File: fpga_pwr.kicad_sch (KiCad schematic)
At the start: 29 parts, among them Q1 BC817, U8 LFE5U-25F-8MG285C

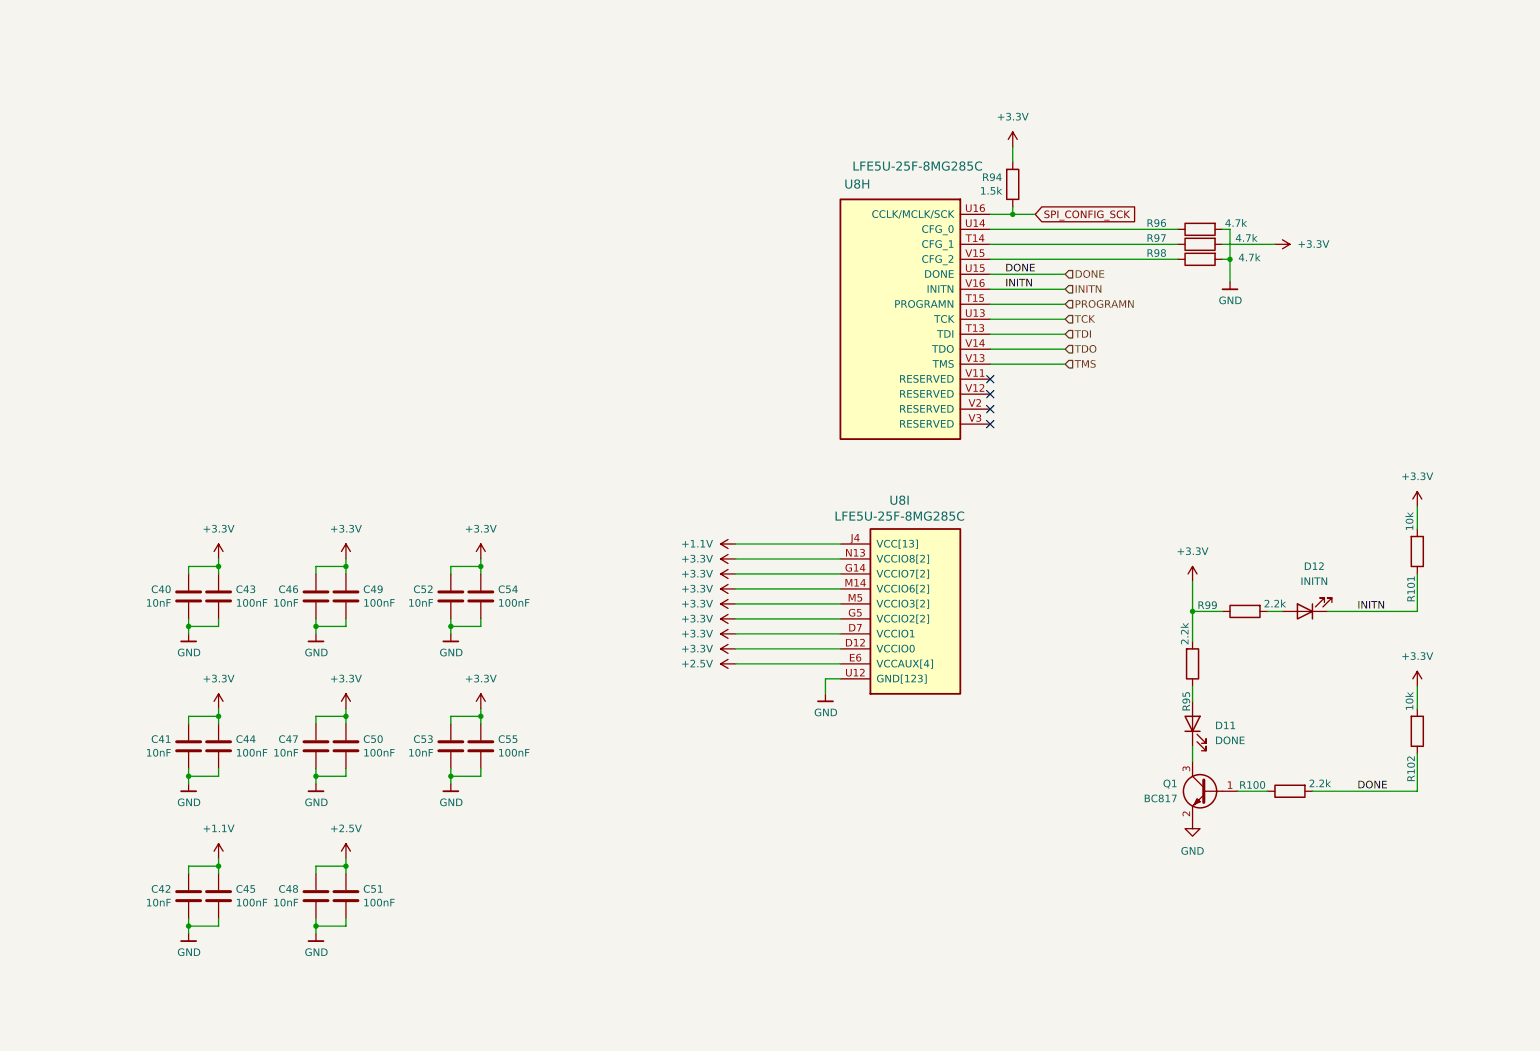
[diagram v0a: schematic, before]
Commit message: Changa fpga footprint to bg256. Update project
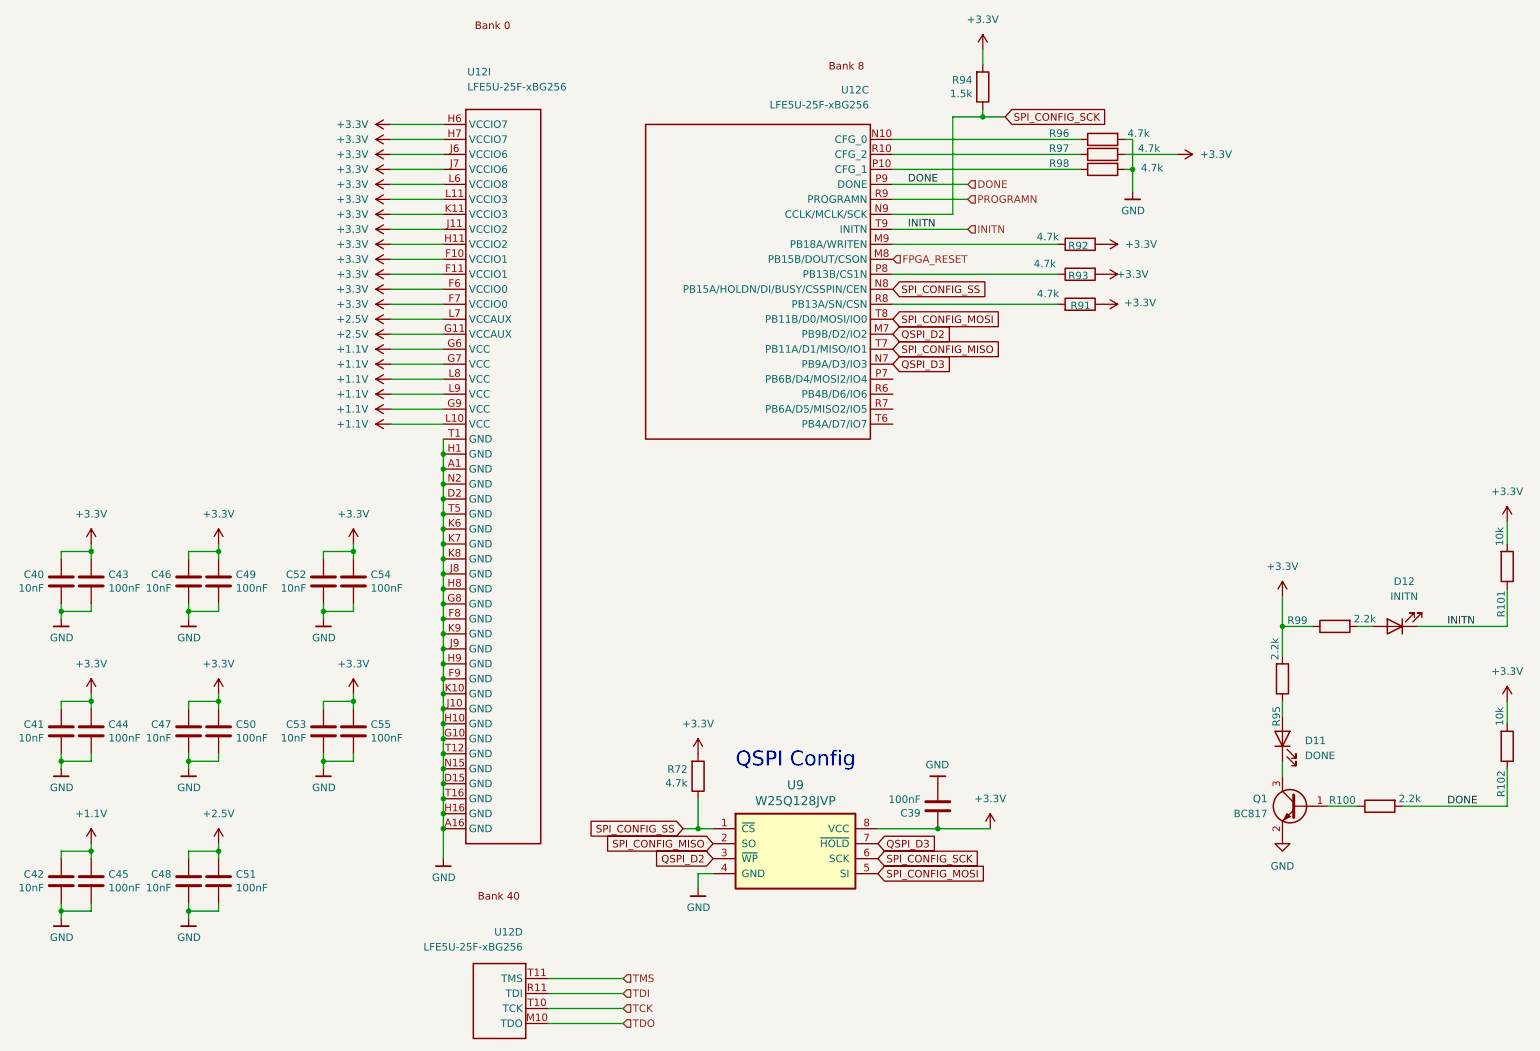
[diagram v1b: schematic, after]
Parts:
- removed U8: LFE5U-25F-8MG285C, kicad:BGA-285, symbol gkl_lattice:ECP5U25-MG285
- added C39: 100nF, Capacitor_SMD:C_0603_1608Metric, symbol Device:C
- added R72, R91, R92, R93: 4.7k, Resistor_SMD:R_0603_1608Metric, symbol Device:R
- added U12: LFE5U-25F-xBG256, EasyEDA_Lib:CABGA-256_L14.0-W14.0-R16-C16-P0.80-TL, symbol asterix:LFE5U-25F-BG256
- added U9: W25Q128JVP, Package_SON:WSON-8-1EP_6x5mm_P1.27mm_EP3.4x4mm, symbol gkl_mem:AT25SF081
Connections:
- net +1.1V: now also U12.G6 (VCC), U12.G7 (VCC), U12.G9 (VCC), U12.L10 (VCC), U12.L8 (VCC), U12.L9 (VCC)
- net +2.5V: now also U12.G11 (VCCAUX), U12.L7 (VCCAUX)
- net +3.3V: now also C39.1, R72.2, R91.1, R92.2, R93.2, U12.F10 (VCCIO1), U12.F11 (VCCIO1), U12.F6 (VCCIO0), U12.F7 (VCCIO0), U12.H11 (VCCIO2), U12.H6 (VCCIO7), U12.H7 (VCCIO7), U12.J11 (VCCIO2), U12.J6 (VCCIO6), U12.J7 (VCCIO6), U12.K11 (VCCIO3), U12.L11 (VCCIO3), U12.L6 (VCCIO8), U9.8 (VCC)
- net DONE: now also U12.P9 (DONE)
- net GND: now also C39.2, U12.A1 (GND), U12.A16 (GND), U12.D15 (GND), U12.D2 (GND), U12.F8 (GND), U12.F9 (GND), U12.G10 (GND), U12.G8 (GND), U12.H1 (GND), U12.H10 (GND), U12.H16 (GND), U12.H8 (GND), U12.H9 (GND), U12.J10 (GND), U12.J8 (GND), U12.J9 (GND), U12.K10 (GND), U12.K6 (GND), U12.K7 (GND), U12.K8 (GND), U12.K9 (GND), U12.N15 (GND), U12.N2 (GND), U12.T1 (GND), U12.T12 (GND), U12.T16 (GND), U12.T5 (GND), U9.4 (GND)
- net INITN: now also U12.T9 (INITN)
- net PROGRAMN: now also U12.R9 (PROGRAMN)
- net SPI_CONFIG_SCK: now also U12.N9 (CCLK/MCLK/SCK), U9.6 (SCK)
- net TCK: now also U12.T10 (TCK)
- net TDI: now also U12.R11 (TDI)
- net TDO: now also U12.M10 (TDO)
- net TMS: now also U12.T11 (TMS)
- net at R97.1: now also U12.R10 (CFG_2)
- net at R96.1: now also U12.N10 (CFG_0)
- net at R98.1: now also U12.P10 (CFG_1)
- new net: R91.2, U12.R8 (PB13A/SN/CSN)
- new net: R92.1, U12.M9 (PB18A/WRITEN)
- new net: R93.1, U12.P8 (PB13B/CS1N)
- new net FPGA_RESET: U12.M8 (PB15B/DOUT/CSON)
- new net QSPI_D2: U12.M7 (PB9B/D2/IO2), U9.3 (~{WP})
- new net QSPI_D3: U12.N7 (PB9A/D3/IO3), U9.7 (~{HOLD})
- new net SPI_CONFIG_MISO: U12.T7 (PB11A/D1/MISO/IO1), U9.2 (SO)
- new net SPI_CONFIG_MOSI: U12.T8 (PB11B/D0/MOSI/IO0), U9.5 (SI)
- new net SPI_CONFIG_SS: R72.1, U12.N8 (PB15A/HOLDN/DI/BUSY/CSSPIN/CEN), U9.1 (~{CS})
- no-connect marks 4 -> 0
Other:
- note added: "QSPI Config"
- moved on the sheet: C40, C41, C42, C43, C44, C45, C46, C47, C48, C49, C50, C51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
